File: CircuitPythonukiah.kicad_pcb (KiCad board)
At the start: 2 copper layers, 193 x 169 mm, 25 parts, among them J1 USB_B_Micro, SW1 SW_DIP_x01, SW2 SW_DIP_x01, U1 TinyS2

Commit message: Add KiCAD files
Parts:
- G***: value OSHW-logo_silkscreen-back_18mm -> OSHW Logo 18mm; footprint OSHWA:OSHW-logo_silkscreen-back_18mm -> CircuitPythonukiah:OSHW Logo 18mm
- LS1: footprint Adafruit:Piezo Buzzer -> CircuitPythonukiah:Piezo Buzzer
- U1: footprint Unexpected Maker:TinyS2 -> CircuitPythonukiah:TinyS2
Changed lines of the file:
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@@
     (pad "" np_thru_hole circle (at 0 0) (size 6.4 6.4) (drill 6.4) (layers *.Cu *.Mask))
   )
-  (footprint "Unexpected Maker:TinyS2" (layer "F.Cu")
+  (footprint "CircuitPythonukiah:TinyS2" (layer "F.Cu")
     (at 128.164258 144.674258 90)
     (property "Sheetfile" "AutoMenorah.kicad_sch")
     (property "Sheetname" "")
     (attr through_hole)
-    (fp_text reference "U1" (at -11.535742 0.105742 unlocked) (layer "F.SilkS")
+    (fp_text reference "U1" (at 0 -15.24 90 unlocked) (layer "F.SilkS")
       (effects (font (size 1 1) (thickness 0.15)))
     )
@@
     )
   )
-  (footprint "Adafruit:Piezo Buzzer" (layer "F.Cu")
+  (footprint "CircuitPythonukiah:Piezo Buzzer" (layer "F.Cu")
     (at 128.164258 109.114258)
     (property "Sheetfile" "AutoMenorah.kicad_sch")
@@
     )
   )
-  (footprint "OSHWA:OSHW-logo_silkscreen-back_18mm" (layer "B.Cu")
+  (footprint "CircuitPythonukiah:OSHW Logo 18mm" (layer "B.Cu")
     (at 128.143 84.201 180)
     (fp_text reference "G***" (at 0 -9.54532) (layer "B.SilkS") hide
       (effects (font (size 0.82042 0.82042) (thickness 0.16256)) (justify mirror))
     )
-    (fp_text value "OSHW-logo_silkscreen-back_18mm" (at 0 9.54532) (layer "B.SilkS") hide
+    (fp_text value "OSHW Logo 18mm" (at 0 9.54532) (layer "B.SilkS") hide
       (effects (font (size 0.82042 0.82042) (thickness 0.16256)) (justify mirror))
     )

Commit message: Update repo with currnt work
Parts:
- removed SW2: SW_DIP_x01, Button_Switch_SMD:SW_DIP_SPSTx01_Slide_6.7x4.1mm_W8.61mm_P2.54mm_LowProfile
- J1: footprint Connector_USB:USB_Micro-B_Wuerth_614105150721_Vertical_CircularHoles -> CUI Devices:CUI_UJC-VP-3-SMT-TR
- LS1: footprint CircuitPythonukiah:Piezo Buzzer -> Adafruit:Piezo Buzzer
- M5: renamed from REF**; value MountingHole_6.4mm_M6 -> MountingHole_5.3mm_M5; footprint MountingHole:MountingHole_6.4mm_M6 -> MountingHole:MountingHole_5.3mm_M5
- R1, R2, R3, R4, R5, R6, R7, R8, R9: value 10K -> 100; footprint Resistor_SMD:R_0805_2012Metric_Pad1.20x1.40mm_HandSolder -> Resistor_THT:R_Axial_DIN0207_L6.3mm_D2.5mm_P7.62mm_Horizontal
- SW1: footprint Button_Switch_SMD:SW_DIP_SPSTx01_Slide_6.7x4.1mm_W8.61mm_P2.54mm_LowProfile -> E-Switch:EG1218
- U1: value TinyS2 -> QT_Py; footprint CircuitPythonukiah:TinyS2 -> Adafruit:QT Py
- moved G*** 12.4 mm to (128.3, 71.8)
- moved SW1 9.40 mm to (128.3, 98.3)
- moved LS1 7.73 mm to (128.3, 116.8)
- moved R8 6.73 mm to (147.3, 123.1)
- moved R4 6.54 mm to (109.2, 61.6)
- moved R9 6.52 mm to (128.3, 49.5)
- moved R3 6.52 mm to (109.2, 82.5)
- moved R2 6.51 mm to (109.2, 102.8)
- moved R5 6.48 mm to (147.3, 61.6)
- moved R7 6.46 mm to (147.3, 102.9)
- moved R6 6.46 mm to (147.3, 82.4)
- moved R1 6.25 mm to (109.2, 123.2)
- moved M5 2.54 mm to (128.3, 172.7)
- moved U1 1.38 mm to (128.3, 146.1)
- moved J1 1.32 mm to (128.3, 189.5)
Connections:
- SW1 pad 1: 3V -> MUTE_BTN
- SW1 pad 2: MUTE_BTN -> 3V
- U1 pad 1: unconnected-(U1-Pad1) -> 5V
- U1 pad 10: unconnected-(U1-Pad10) -> SHAMASH
- U1 pad 11: unconnected-(U1-Pad11) -> LED5
- U1 pad 12: unconnected-(U1-Pad12) -> LED6
- U1 pad 13: unconnected-(U1-Pad13) -> LED7
- U1 pad 14: unconnected-(U1-Pad14) -> LED8
- U1 pad 3: 5V -> 3V
- U1 pad 4: 3V -> LED4
- U1 pad 5: SHAMASH -> LED3
- U1 pad 6: SPKR -> LED2
- U1 pad 7: MUTE_BTN -> LED1
- U1 pad 8: LED_DIR_BTN -> SPKR
- U1 pad 9: unconnected-(U1-Pad9) -> MUTE_BTN
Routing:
- net LED_DIR_BTN: track 84.7 -> 0.00 mm, vias 1 -> 0
- net 3V: track 87.7 -> 64.4 mm, vias 1 -> 0
- net LED1: track 42.3 -> 19.7 mm
- net GND: track 956.3 -> 978.4 mm, vias 2 -> 3
- net LED2: track 60.0 -> 43.7 mm
- net SHAMASH: track 113.8 -> 102.2 mm
- net LED3: track 77.7 -> 67.6 mm
- net Net-(D5-Pad2): track 30.7 -> 25.0 mm
- net Net-(D8-Pad2): track 130.6 -> 124.9 mm
- net Net-(D2-Pad2): track 99.8 -> 94.2 mm
- net Net-(D6-Pad2): track 65.5 -> 60.0 mm
- net Net-(D3-Pad2): track 65.0 -> 59.6 mm
- net Net-(D9-Pad2): track 13.1 -> 7.62 mm
- net Net-(D7-Pad2): track 98.6 -> 93.2 mm
- net Net-(D4-Pad2): track 30.3 -> 25.0 mm
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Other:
- board text added: "CircuitPyhthonukiah"
- board text added: "Muted"
- board text added: "Sound"
- board text removed: "CircuitPyhthonukah"

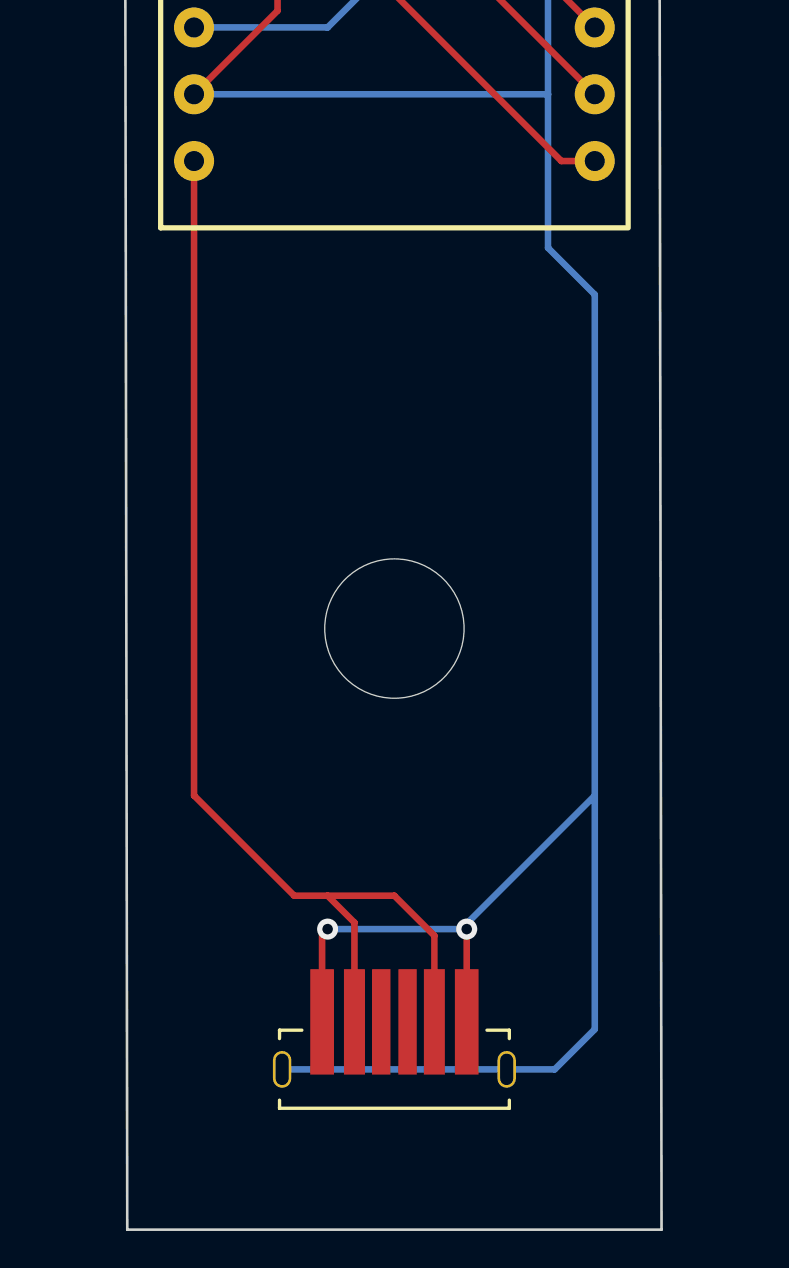
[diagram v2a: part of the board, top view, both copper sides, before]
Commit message: Move USB-C to back side
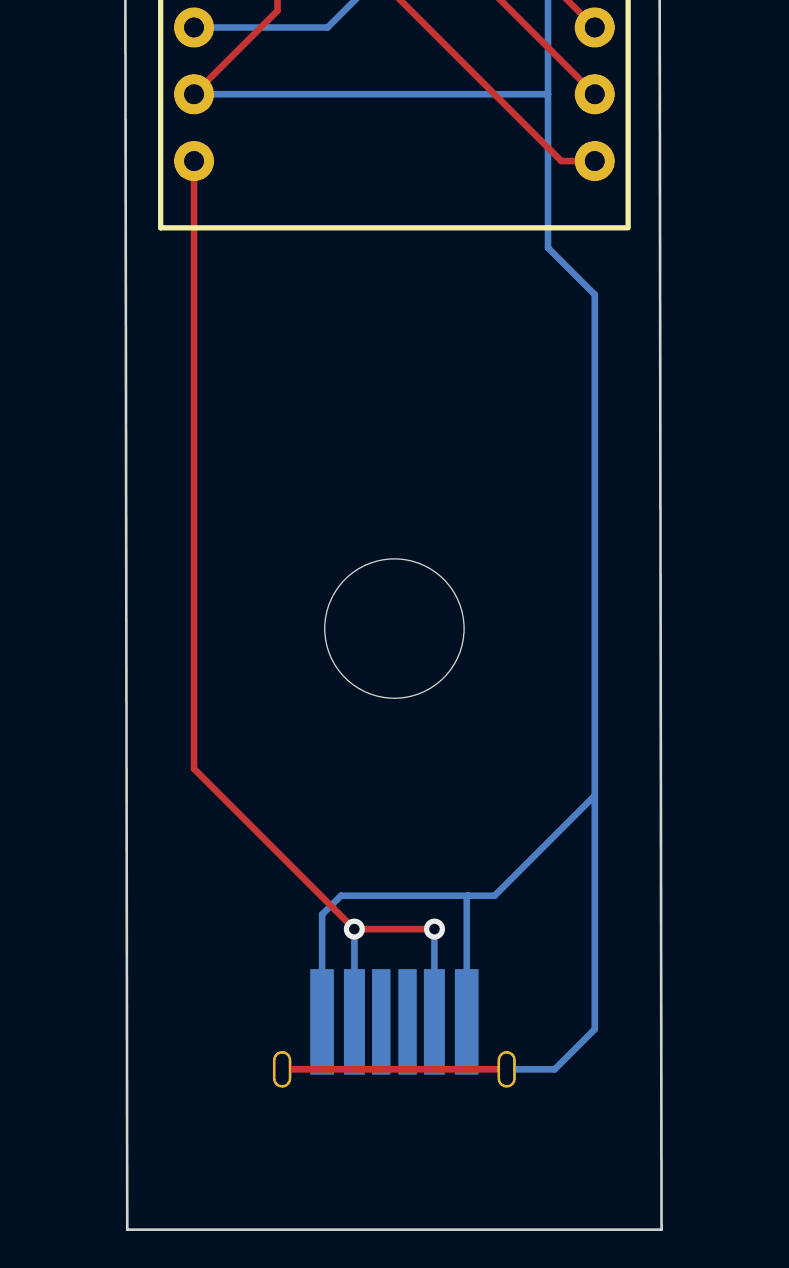
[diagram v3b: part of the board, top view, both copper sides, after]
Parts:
- J1: moved to B.Cu
- turned J1 to 180 degrees
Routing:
- net 5V: track 44.0 -> 41.8 mm, vias 0 -> 2
- net GND: track 978.4 -> 980.0 mm, vias 3 -> 1

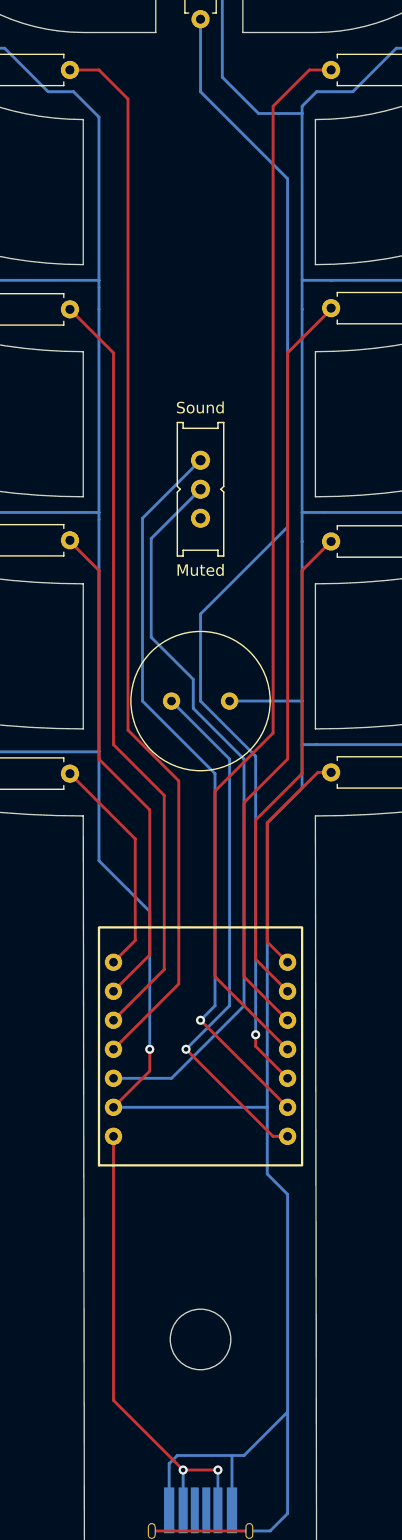
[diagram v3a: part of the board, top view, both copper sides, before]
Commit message: Flip microcontroller for ease of configuring
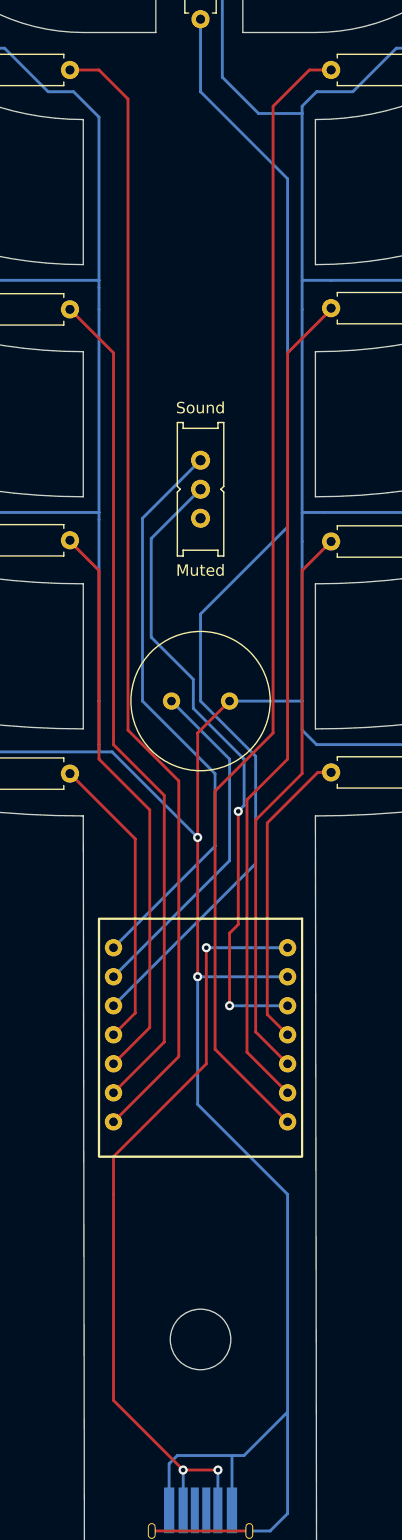
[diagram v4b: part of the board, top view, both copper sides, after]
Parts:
- moved U1 1.27 mm to (128.3, 147.3), turned to -90 degrees
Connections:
- U1 pad 11: LED5 -> LED1
- U1 pad 12: LED6 -> LED2
- U1 pad 13: LED7 -> LED3
- U1 pad 14: LED8 -> LED4
- U1 pad 4: LED4 -> LED8
- U1 pad 5: LED3 -> LED7
- U1 pad 6: LED2 -> LED6
- U1 pad 7: LED1 -> LED5
- U1 pad 8: SPKR -> MUTE_BTN
- U1 pad 9: MUTE_BTN -> SPKR
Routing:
- net 5V: track 41.8 -> 68.8 mm, vias 2 -> 3
- net GND: track 980.0 -> 957.4 mm, vias 1 -> 2
- net SPKR: track 46.2 -> 30.4 mm, vias 1 -> 0
- net MUTE_BTN: track 65.1 -> 51.1 mm, vias 1 -> 0
- net 3V: track 64.4 -> 56.0 mm, vias 0 -> 2
- net LED1: track 19.7 -> 26.0 mm
- net LED8: track 20.2 -> 26.6 mm
- net LED4: track 92.9 -> 99.2 mm
- net LED7: track 43.3 -> 49.6 mm
- net LED5: track 93.7 -> 100.0 mm
- net LED3: track 67.6 -> 74.0 mm
- net LED2: track 43.7 -> 50.0 mm
- net LED6: track 67.1 -> 73.3 mm
- net SHAMASH: track 102.2 -> 99.8 mm, vias 1 -> 0

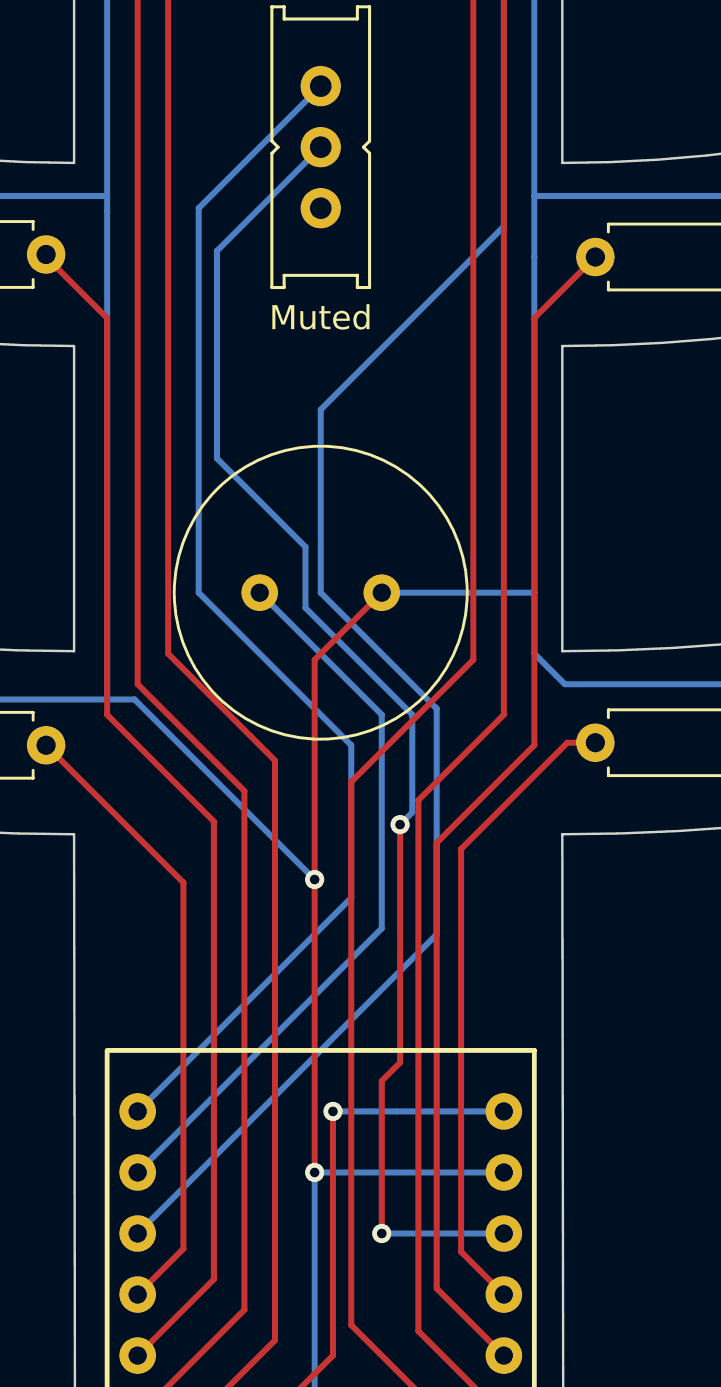
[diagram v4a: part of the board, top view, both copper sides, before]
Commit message: Change A0 to be pull-up input
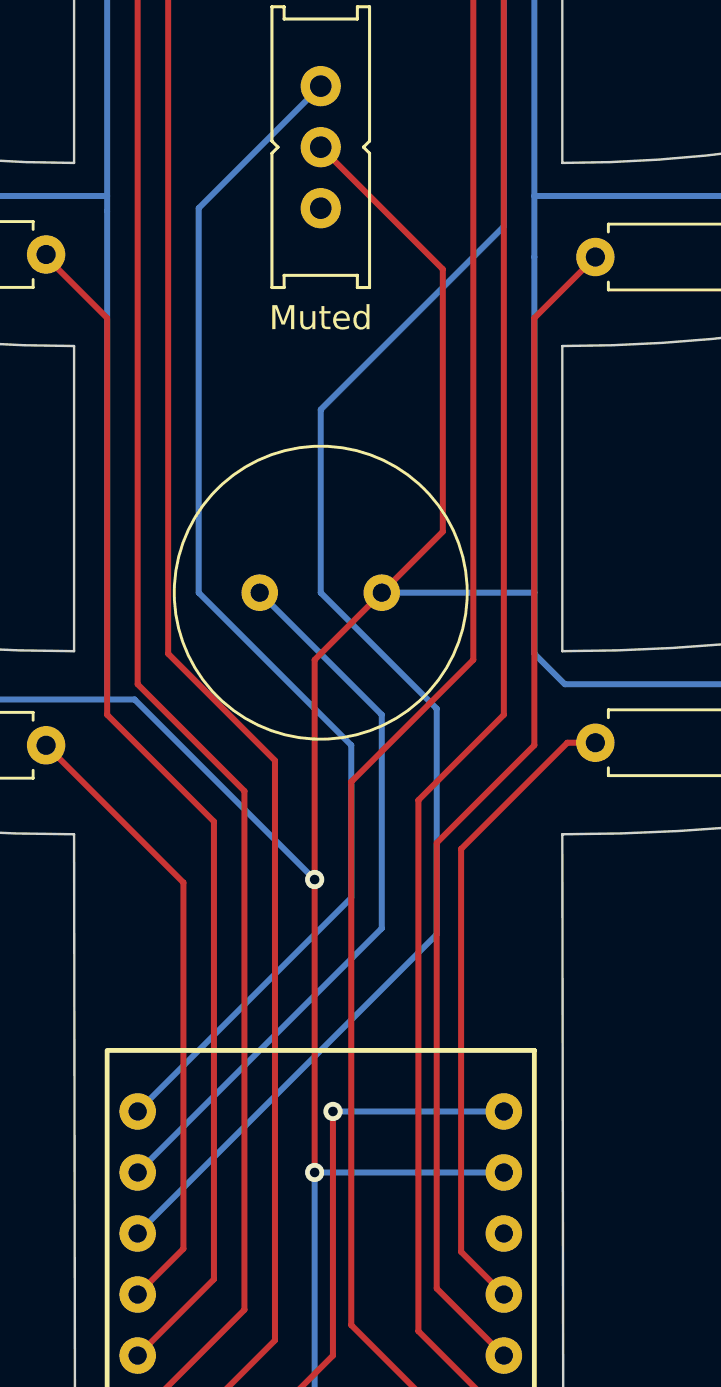
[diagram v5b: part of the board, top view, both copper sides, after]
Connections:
- SW1 pad 2: 3V -> GND
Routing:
- net 3V: track 56.0 -> 0.00 mm, vias 2 -> 0
- net GND: track 957.4 -> 979.1 mm
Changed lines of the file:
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@@
       (net 5 "MUTE_BTN") (pinfunction "A") (pintype "passive"))
     (pad "2" thru_hole circle (at 0 0 270) (size 1.6764 1.6764) (drill 0.9) (layers *.Cu *.Mask)
-      (net 3 "3V") (pinfunction "B") (pintype "passive"))
+      (net 1 "GND") (pinfunction "B") (pintype "passive"))
     (pad "3" thru_hole circle (at 2.54 0 270) (size 1.6764 1.6764) (drill 0.9) (layers *.Cu *.Mask)
       (net 24 "unconnected-(SW1-Pad3)") (pinfunction "C") (pintype "passive"))
@@
   )
   (segment (start 128.016 140.97) (end 128.016 128.778) (width 0.25) (layer "F.Cu") (net 1))
+  (segment (start 128.27 98.298) (end 133.35 103.378) (width 0.25) (layer "F.Cu") (net 1))
   (segment (start 128.016 128.778) (end 128.016 119.634) (width 0.25) (layer "F.Cu") (net 1))
   (segment (start 124 189.484) (end 132.54 189.484) (width 0.25) (layer "F.Cu") (net 1))
+  (segment (start 133.35 103.378) (end 133.35 114.3) (width 0.25) (layer "F.Cu") (net 1))
   (segment (start 128.016 119.634) (end 130.81 116.84) (width 0.25) (layer "F.Cu") (net 1))
+  (segment (start 133.35 114.3) (end 130.81 116.84) (width 0.25) (layer "F.Cu") (net 1))
   (via (at 128.016 140.97) (size 0.8) (drill 0.4) (layers "F.Cu" "B.Cu") (net 1))
   (via (at 128.016 128.778) (size 0.8) (drill 0.4) (layers "F.Cu" "B.Cu") (net 1))
@@
   (segment (start 129.794 184.15) (end 129.79 184.154) (width 0.25) (layer "B.Cu") (net 2))
   (segment (start 129.79 184.154) (end 129.79 187.679) (width 0.25) (layer "B.Cu") (net 2))
-  (segment (start 131.572 126.492) (end 131.572 136.398) (width 0.25) (layer "F.Cu") (net 3))
-  (segment (start 130.81 137.16) (end 130.81 143.51) (width 0.25) (layer "F.Cu") (net 3))
-  (segment (start 131.572 136.398) (end 130.81 137.16) (width 0.25) (layer "F.Cu") (net 3))
-  (via (at 131.572 126.492) (size 0.8) (drill 0.4) (layers "F.Cu" "B.Cu") (net 3))
-  (via (at 130.81 143.51) (size 0.8) (drill 0.4) (layers "F.Cu" "B.Cu") (net 3))
-  (segment (start 128.27 98.298) (end 123.952 102.616) (width 0.25) (layer "B.Cu") (net 3))
-  (segment (start 132.08 125.984) (end 131.572 126.492) (width 0.25) (layer "B.Cu") (net 3))
-  (segment (start 127.635 114.935) (end 127.635 117.475) (width 0.25) (layer "B.Cu") (net 3))
-  (segment (start 130.81 143.51) (end 135.89 143.51) (width 0.25) (layer "B.Cu") (net 3))
-  (segment (start 127.635 117.475) (end 132.08 121.92) (width 0.25) (layer "B.Cu") (net 3))
-  (segment (start 132.08 121.92) (end 132.08 125.984) (width 0.25) (layer "B.Cu") (net 3))
-  (segment (start 123.952 102.616) (end 123.952 111.252) (width 0.25) (layer "B.Cu") (net 3))
-  (segment (start 123.952 111.252) (end 127.635 114.935) (width 0.25) (layer "B.Cu") (net 3))
   (segment (start 133.096 121.666) (end 128.27 116.84) (width 0.25) (layer "B.Cu") (net 4))
   (segment (start 135.89 101.6) (end 135.89 71.12) (width 0.25) (layer "B.Cu") (net 4))
